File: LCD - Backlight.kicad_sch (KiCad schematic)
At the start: 14 parts, among them IC2 TPS61165DBVR

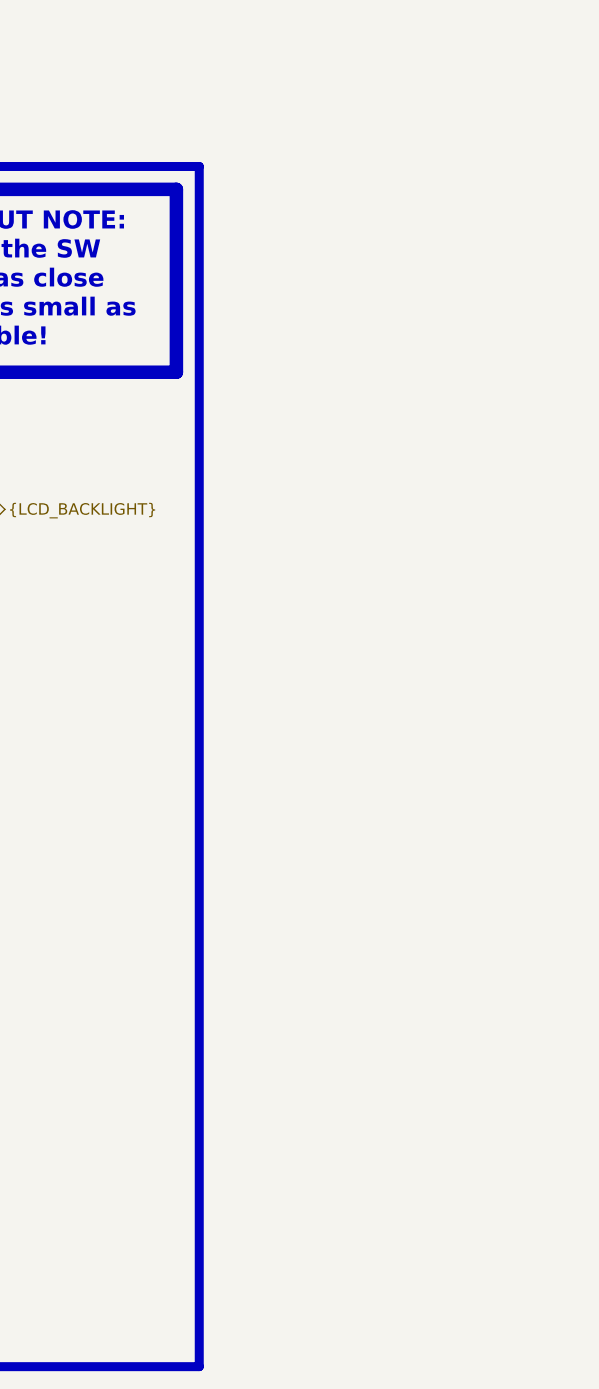
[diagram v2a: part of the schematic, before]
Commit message: added fiducal markers, mounting holes, testpoints
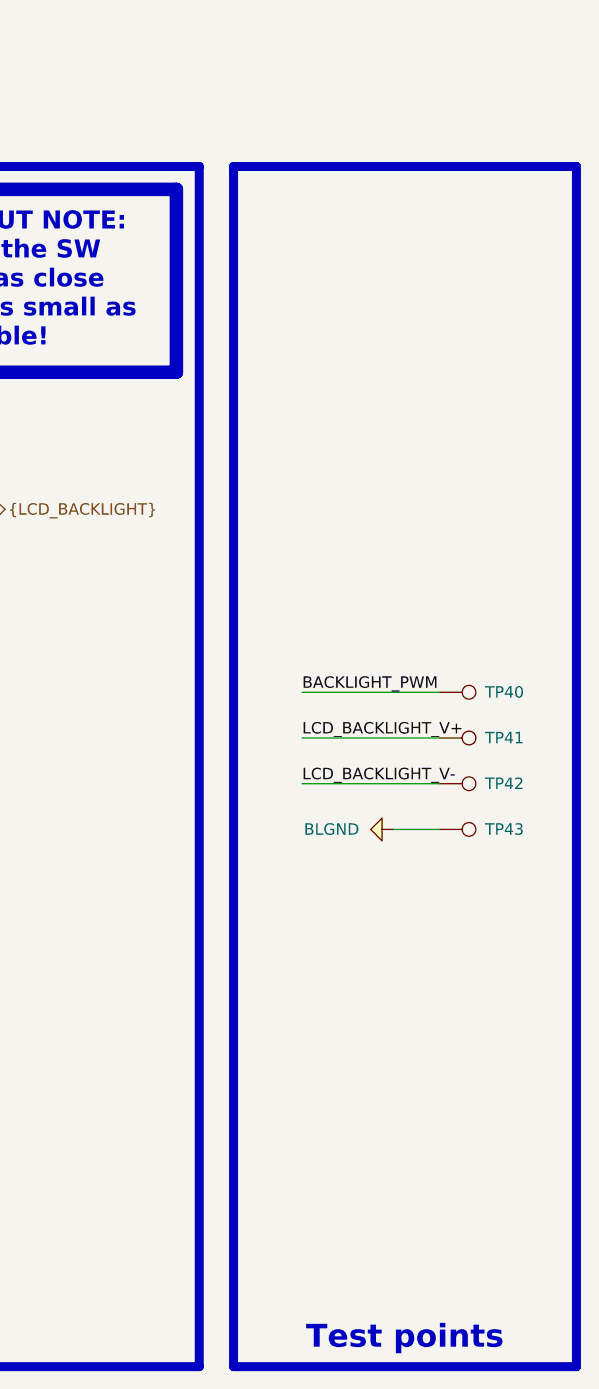
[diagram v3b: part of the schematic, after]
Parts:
- added TP40, TP41, TP42, TP43: TestPoint, 0_pads:TestPoint_Pad_D0.4mm_Back, symbol Connector:TestPoint
- IC2: footprint SOT95P280X145-6N -> (none)
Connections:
- net BACKLIGHT_PWM: now also TP40.1
- net BLGND: now also TP43.1
- net LCD_BACKLIGHT_V+: now also TP41.1
- net LCD_BACKLIGHT_V-: now also TP42.1

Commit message: some visual changes, color of nets etc
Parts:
- IC2: footprint (none) -> 0_integrated_circuits:SOT95P280X145-6N
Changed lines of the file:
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@@
 			)
 		)
-		(property "Footprint" ""
+		(property "Footprint" "0_integrated_circuits:SOT95P280X145-6N"
 			(at 264.16 197.79 0)
 			(effects

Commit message: test points, colors, drc
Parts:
- TP40, TP41, TP42, TP43: footprint 0_pads:TestPoint_Pad_D0.4mm_Back -> 0_pads:TestPoint_Pad_D0.5mm_Back
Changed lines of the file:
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@@
 			)
 		)
-		(property "Footprint" "0_pads:TestPoint_Pad_D0.4mm_Back"
+		(property "Footprint" "0_pads:TestPoint_Pad_D0.5mm_Back"
 			(at 378.46 133.35 0)
 			(effects
@@
 			)
 		)
-		(property "Footprint" "0_pads:TestPoint_Pad_D0.4mm_Back"
+		(property "Footprint" "0_pads:TestPoint_Pad_D0.5mm_Back"
 			(at 378.46 123.19 0)
 			(effects
@@
 			)
 		)
-		(property "Footprint" "0_pads:TestPoint_Pad_D0.4mm_Back"
+		(property "Footprint" "0_pads:TestPoint_Pad_D0.5mm_Back"
 			(at 378.46 138.43 0)
 			(effects
@@
 			)
 		)
-		(property "Footprint" "0_pads:TestPoint_Pad_D0.4mm_Back"
+		(property "Footprint" "0_pads:TestPoint_Pad_D0.5mm_Back"
 			(at 378.46 128.27 0)
 			(effects

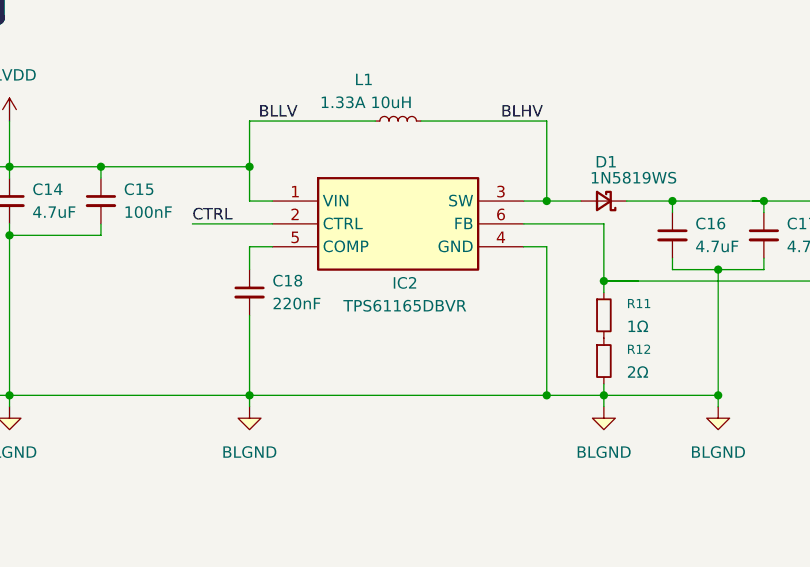
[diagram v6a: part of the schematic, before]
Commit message: designator chagnes and cleanup silkscreen
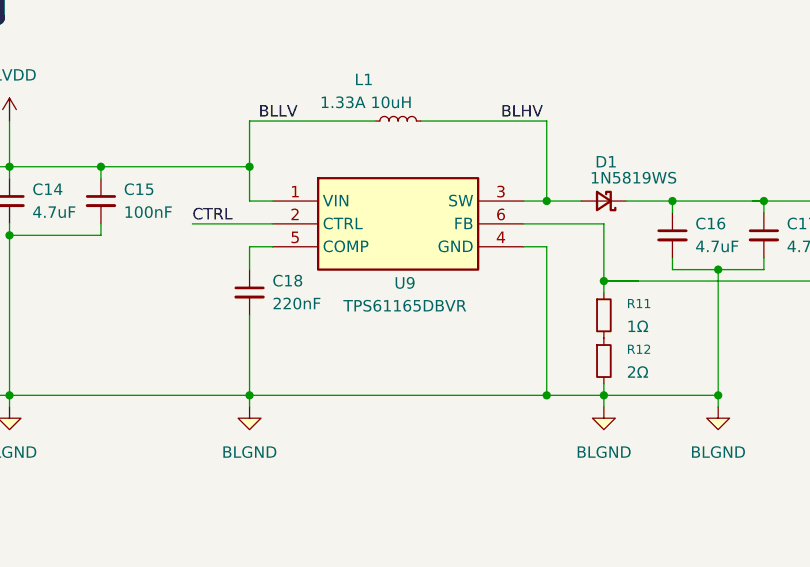
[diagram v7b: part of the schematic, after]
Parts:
- C14, C16, C17: LCSC PN (none) -> C1779
- C15: LCSC PN (none) -> C1525
- C18: LCSC PN (none) -> C16772
- D1: LCSC PN (none) -> C191023
- L1: LCSC PN (none) -> C518881
- L2, L3: LCSC PN (none) -> C1017
- R10: LCSC PN (none) -> C25744
- R11: LCSC PN (none) -> C22936
- R12: LCSC PN (none) -> C22977
- R9: LCSC PN (none) -> C17168
- U9: renamed from IC2; footprint 0_integrated_circuits:SOT95P280X145-6N -> SOT95P280X145-6N; LCSC PN (none) -> C58756
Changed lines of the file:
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@@
+			)
+		)
+		(property "LCSC PN" "C1779"
+			(at 210.82 102.87 0)
+			(effects
+				(font
+					(size 1.27 1.27)
+				)
+				(hide yes)
 			)
 		)
@@
 			)
 		)
+		(property "LCSC PN" "C1779"
+			(at 294.64 106.68 0)
+			(effects
+				(font
+					(size 1.27 1.27)
+				)
+				(hide yes)
+			)
+		)
 		(pin "2"
 		)
@@
 			)
 		)
+		(property "LCSC PN" "C22977"
+			(at 276.86 120.65 0)
+			(effects
+				(font
+					(size 1.27 1.27)
+				)
+				(hide yes)
+			)
+		)
 		(pin "2"
 		)
@@
 		)
 		(property "Supplier Part Number 1" "C1017"
+			(at 201.93 99.06 0)
+			(effects
+				(font
+					(size 1.27 1.27)
+				)
+				(hide yes)
+			)
+		)
+		(property "LCSC PN" "C1017"
 			(at 201.93 99.06 0)
 			(effects
@@
 			)
 		)
-		(property "Description" "Resistor, small symbol"
+		(property "Description" "50V ±800ppm/℃ ±1% 0Ω 0402"
 			(at 130.81 113.03 0)
 			(effects
@@
 			)
 		)
+		(property "LCSC PN" "C17168"
+			(at 130.81 113.03 0)
+			(effects
+				(font
+					(size 1.27 1.27)
+				)
+				(hide yes)
+			)
+		)
 		(pin "2"
 		)
@@
 		)
 		(property "Supplier Part Number 1" "C518881"
+			(at 254 93.98 0)
+			(effects
+				(font
+					(size 1.27 1.27)
+				)
+				(hide yes)
+			)
+		)
+		(property "LCSC PN" "C518881"
 			(at 254 93.98 0)
 			(effects
@@
 			)
 		)
+		(property "LCSC PN" "C1525"
+			(at 220.98 102.87 0)
+			(effects
+				(font
+					(size 1.27 1.27)
+				)
+				(hide yes)
+			)
+		)
 		(pin "2"
 		)
@@
 		(on_board yes)
 		(dnp no)
-		(property "Reference" "IC2"
+		(property "Reference" "U9"
 			(at 254.762 112.014 0)
 			(effects
@@
 			)
 		)
-		(property "Footprint" "0_integrated_circuits:SOT95P280X145-6N"
+		(property "Footprint" "SOT95P280X145-6N"
 			(at 264.16 197.79 0)
 			(effects
@@
 			)
 		)
+		(property "LCSC PN" "C58756"
+			(at 240.03 102.87 0)
+			(effects
+				(font
+					(size 1.27 1.27)
+				)
+				(hide yes)
+			)
+		)
 		(pin "1"
 		)
@@
 			(project ""
 				(path "/0650c7a8-acba-429c-9f8e-eec0baf0bc1c/fede4c36-00cc-4d3d-b71c-5243ba232202/d532fde6-fcc8-4703-b00a-b5308b206554"
-					(reference "IC2")
+					(reference "U9")
 					(unit 1)
 				)
@@
 			)
 		)
+		(property "LCSC PN" "C1017"
+			(at 201.93 124.46 0)
+			(effects
+				(font
+					(size 1.27 1.27)
+				)
+				(hide yes)
+			)
+		)
 		(pin "2"
 		)
@@
 			)
 		)
+		(property "LCSC PN" "C22936"
+			(at 276.86 115.57 0)
+			(effects
+				(font
+					(size 1.27 1.27)
+				)
+				(hide yes)
+			)
+		)
 		(pin "1"
 		)
@@
 			)
 		)
-		(property "Description" "Resistor, small symbol"
+		(property "Description" "50V ±100ppm/℃ ±1% 10kΩ 0402"
 			(at 137.16 119.38 0)
 			(effects
@@
 		)
 		(property "Supplier Part Number 1" "C25744"
+			(at 137.16 119.38 0)
+			(effects
+				(font
+					(size 1.27 1.27)
+				)
+				(hide yes)
+			)
+		)
+		(property "LCSC PN" "C25744"
 			(at 137.16 119.38 0)
 			(effects
@@
 			)
 		)
+		(property "LCSC PN" "C16772"
+			(at 237.49 113.03 0)
+			(effects
+				(font
+					(size 1.27 1.27)
+				)
+				(hide yes)
+			)
+		)
 		(pin "1"
 		)
@@
 			)
 		)
+		(property "LCSC PN" "C191023"
+			(at 276.86 102.87 0)
+			(effects
+				(font
+					(size 1.27 1.27)
+				)
+				(hide yes)
+			)
+		)
 		(pin "1"
 		)
@@
 			(at 284.48 106.68 0)
 			(effects
+				(font
+					(size 1.27 1.27)
+				)
+				(hide yes)
+			)
+		)
+		(property "LCSC PN" "C1779"
+			(at 284.48 106.68 0)
+			(effects
